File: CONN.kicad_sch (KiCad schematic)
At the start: 8 parts, among them J1 mot0, J2 encoder0, J3 spare_pins, U5 USBLC6-2SC6

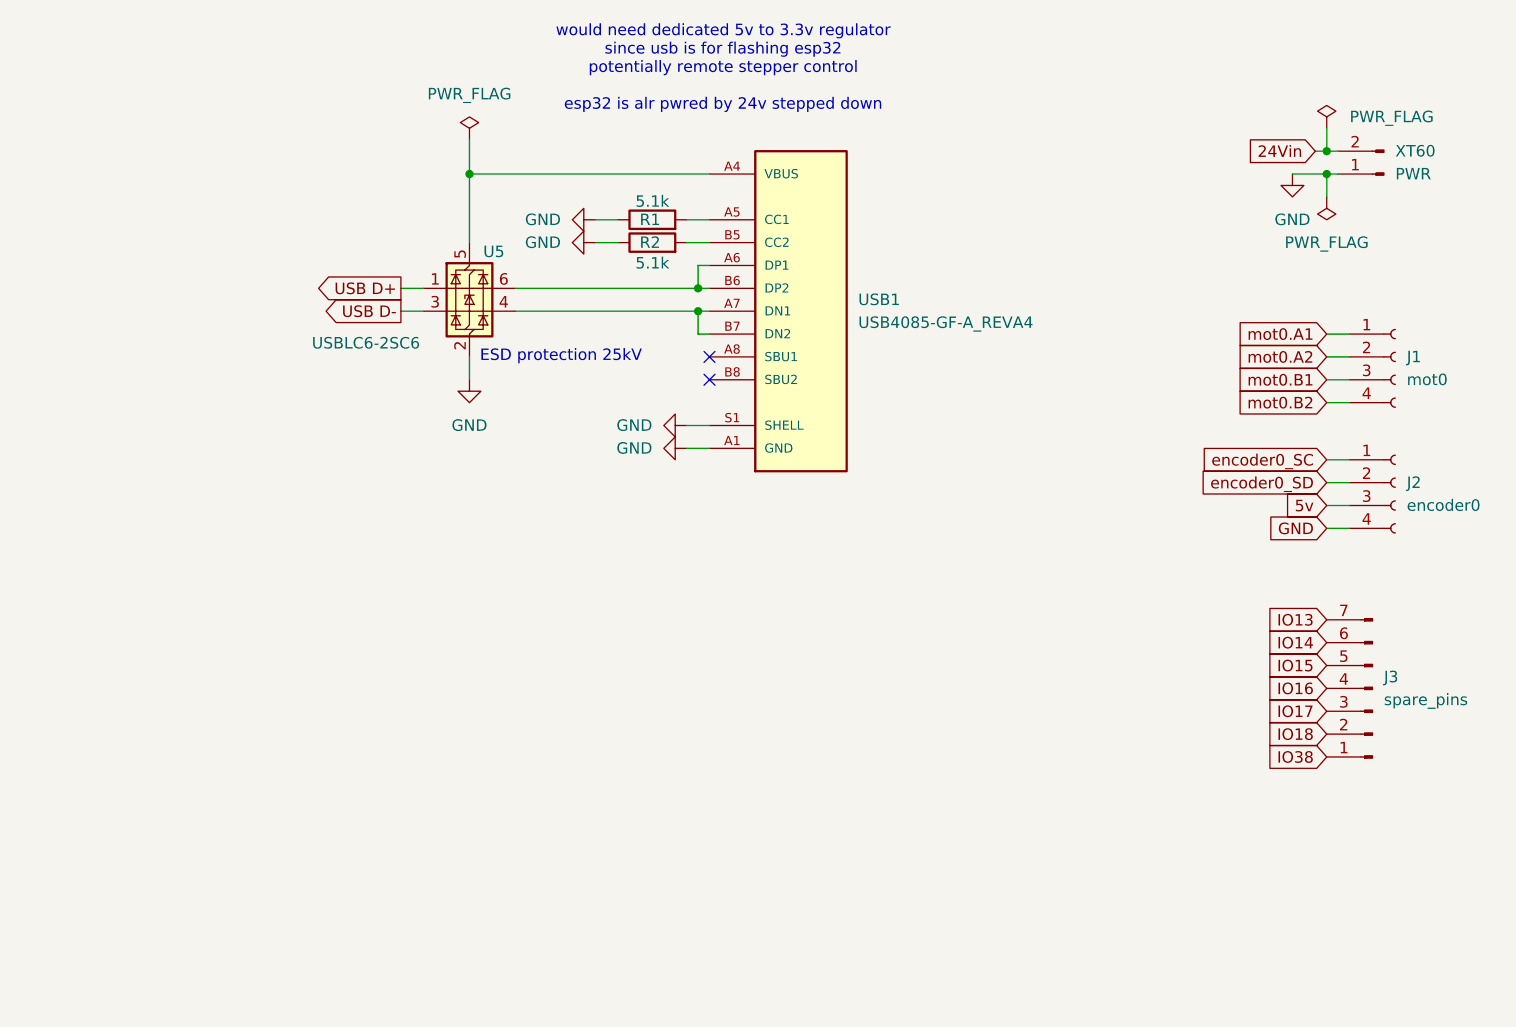
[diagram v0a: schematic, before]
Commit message: revision 1: I2C pullups, USB LDO, etc.
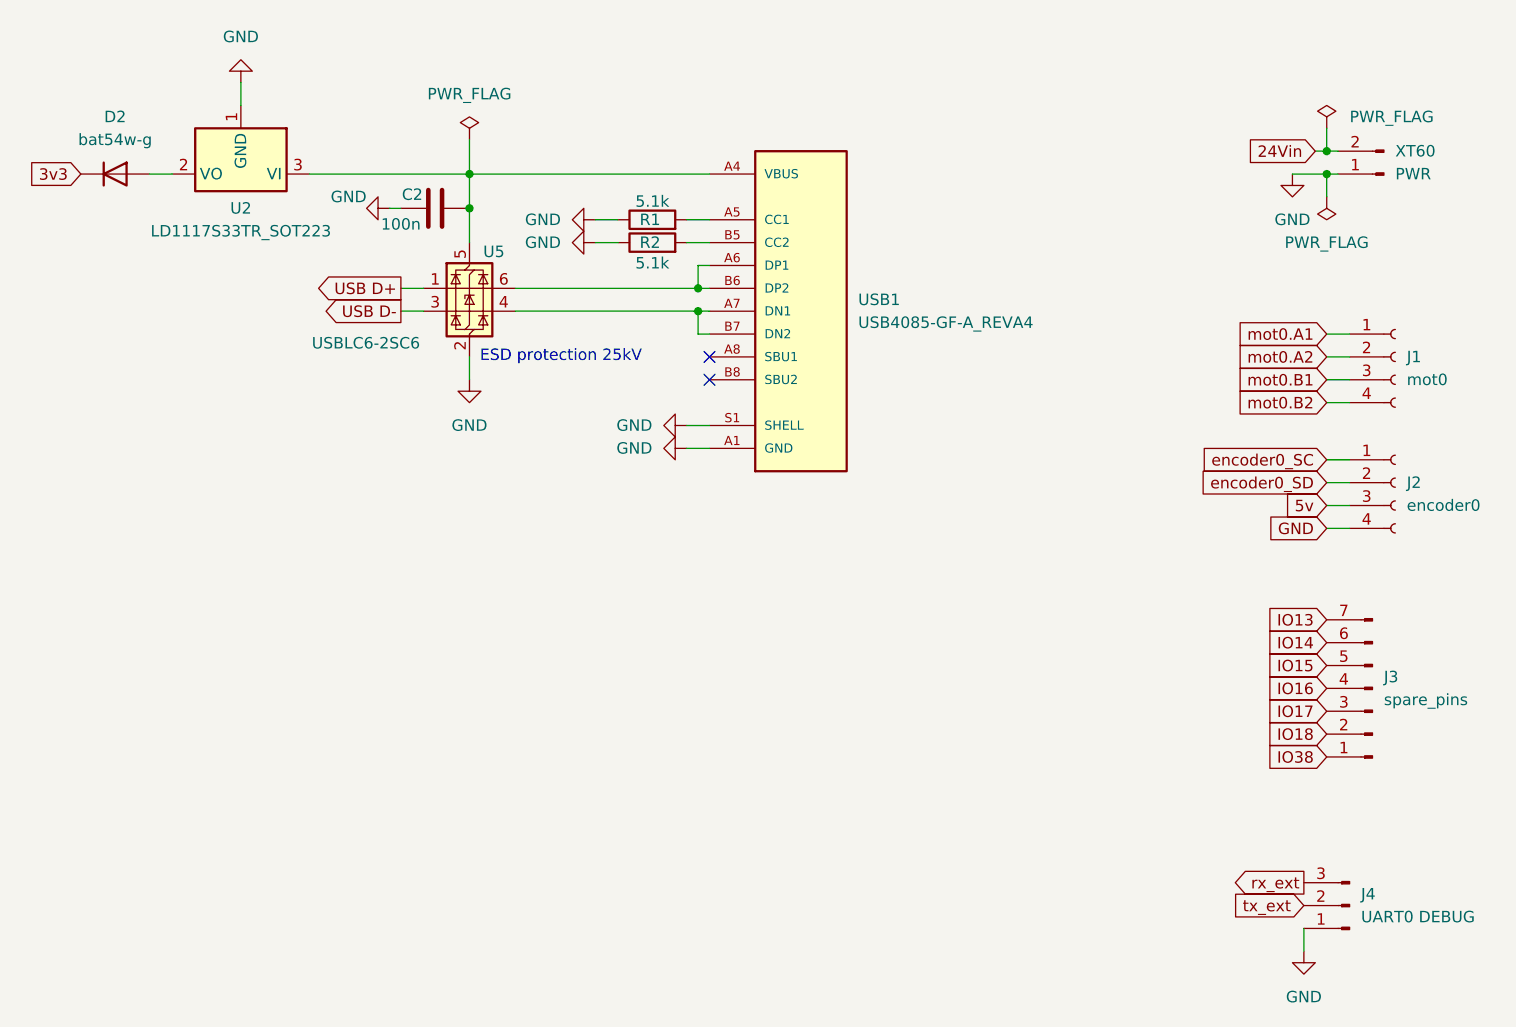
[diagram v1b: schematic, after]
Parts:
- added C2: 100n, symbol Device:C
- added D2: bat54w-g, symbol Device:D
- added J4: UART0 DEBUG, symbol Connector:Conn_01x03_Pin
- added U2: LD1117S33TR_SOT223, Package_TO_SOT_SMD:SOT-223-3_TabPin2, symbol Regulator_Linear:LD1117S33TR_SOT223
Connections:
- net GND: now also C2.1, J4.1 (Pin_1), U2.1 (GND)
- net VBUS: now also C2.2, U2.3 (VI)
- new net: D2.2 (A), U2.2 (VO)
- new net 3v3: D2.1 (K)
- new net rx_ext: J4.3 (Pin_3)
- new net tx_ext: J4.2 (Pin_2)
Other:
- note removed: "would need dedicated 5v to 3.3v regulator since usb is for flashing esp32 potentially remote stepper control esp32 is alr pwred by 24v stepped down"
